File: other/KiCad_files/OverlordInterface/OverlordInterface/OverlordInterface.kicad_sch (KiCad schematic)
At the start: 8 parts, among them J1 Conn_01x12_Female, J2 DE9_Receptacle_MountingHoles_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, J3 DE9_Receptacle_MountingHoles_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, J4 DE9_Receptacle_MountingHoles_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, J5 DE9_Receptacle_MountingHoles_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

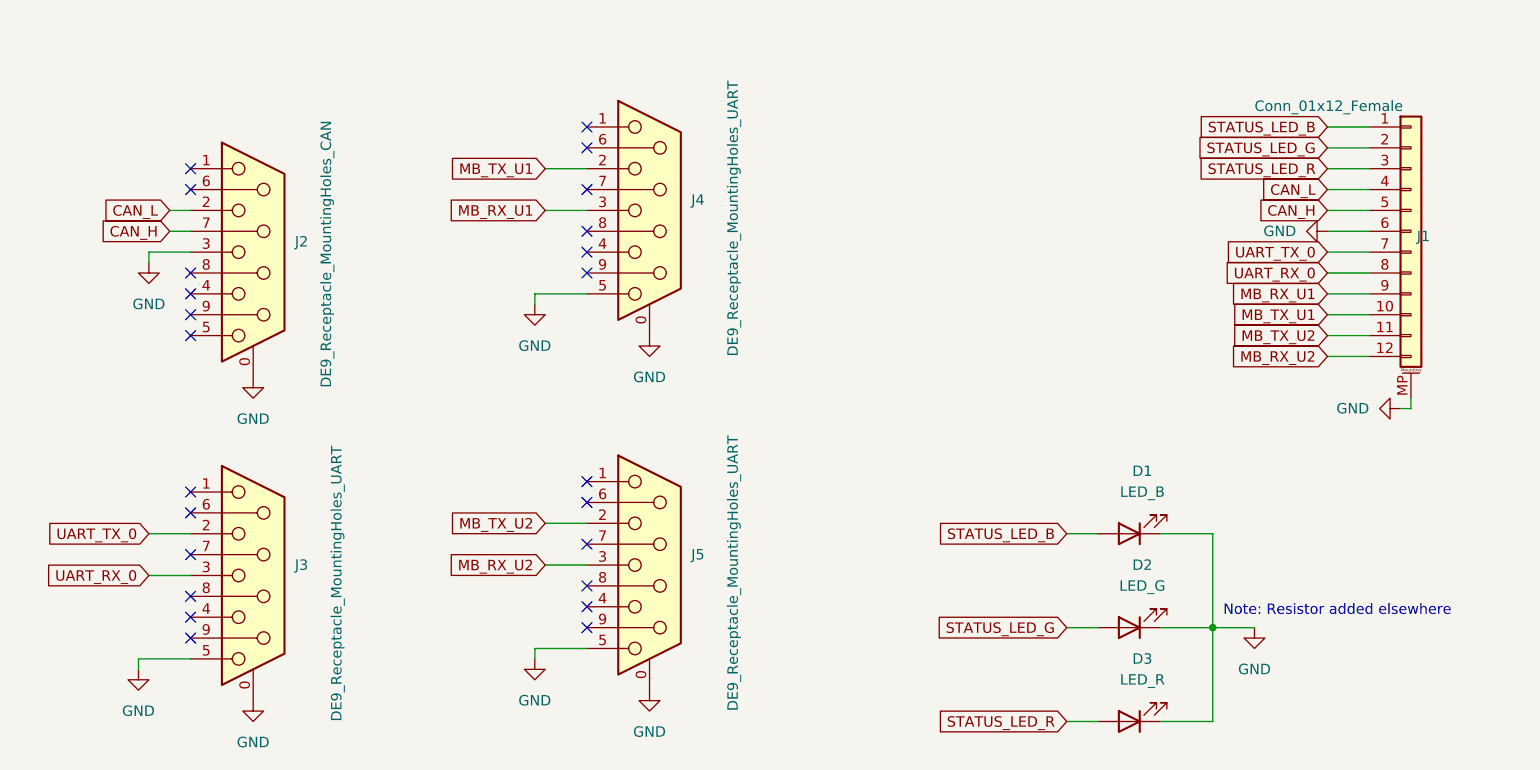
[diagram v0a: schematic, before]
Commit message: sent to production
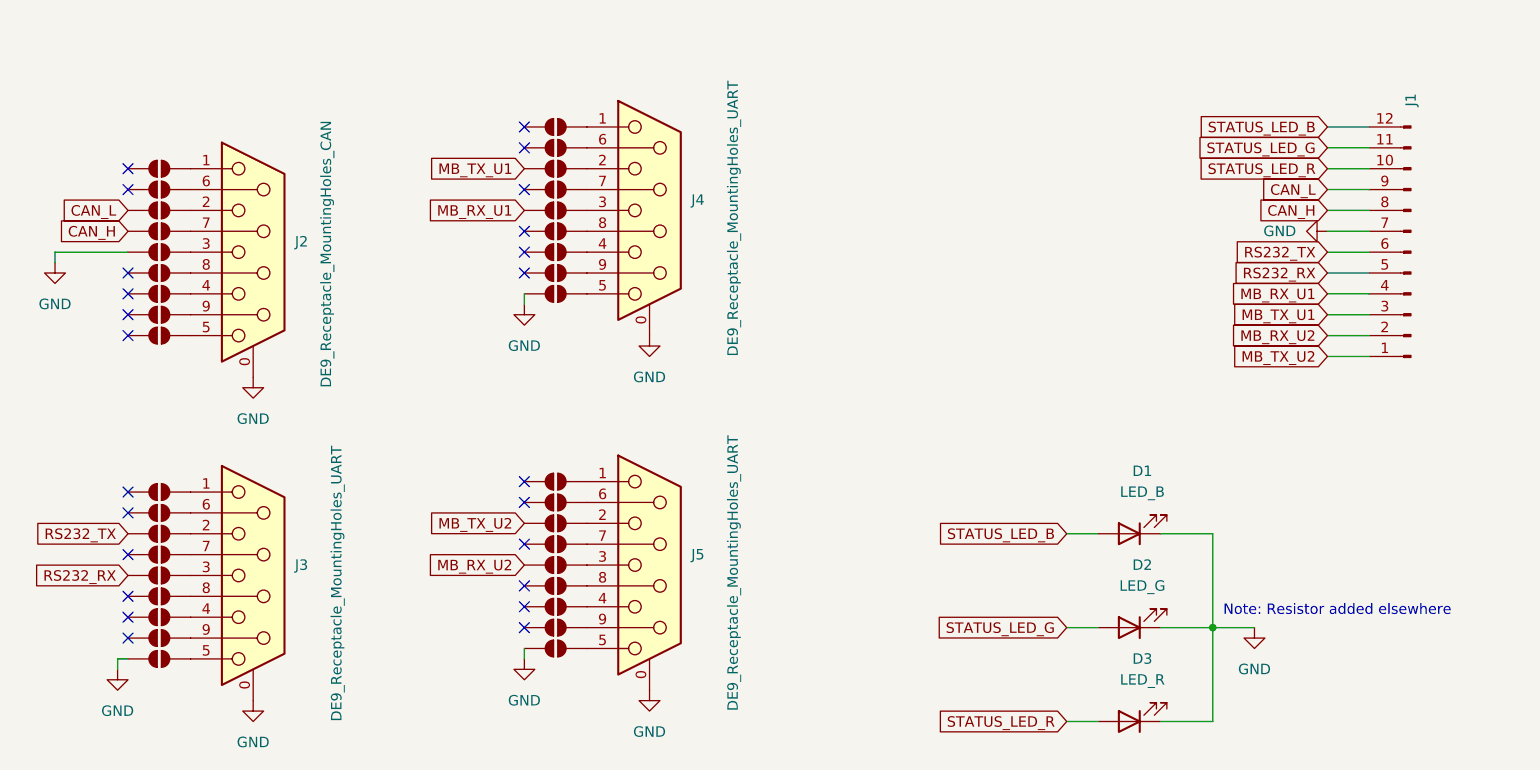
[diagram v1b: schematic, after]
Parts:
- removed J1: Conn_01x12_Female, Connector_Molex:Molex_CLIK-Mate_502386-1270_1x12-1MP_P1.25mm_Horizontal, symbol Connector_Generic_MountingPin:Conn_01x12_MountingPin
- added J1: Conn_01x12_Pin, Connector_Molex:Molex_Picoflex_90325-0012_2x06_P1.27mm_Vertical, symbol Connector:Conn_01x12_Pin
- added JP1, JP10, JP11, JP12, JP13, JP14, JP15, JP16, JP17, JP18, JP19, JP2, JP20, JP21, JP22, JP23, JP24, JP25, JP26, JP27, JP28, JP29, JP3, JP30, JP31, JP32, JP33, JP34, JP35, JP36, JP4, JP5, JP6, JP7, JP8, JP9: SolderJumper_2_Open, Jumper:SolderJumper-2_P1.3mm_Open_RoundedPad1.0x1.5mm, symbol Jumper:SolderJumper_2_Open
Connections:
- net CAN_H: now also J1.8 (Pin_8), JP12.1 (A); no longer J2.7
- net CAN_L: now also J1.9 (Pin_9), JP11.1 (A); no longer J2.2
- net GND: now also J1.7 (Pin_7), JP13.1 (A), JP26.1 (A), JP35.1 (A), JP36.1 (A); no longer J2.3, J3.5, J4.5, J5.5
- net MB_RX_U1: now also J1.4 (Pin_4), JP22.1 (A); no longer J4.3
- net MB_RX_U2: now also J1.2 (Pin_2), JP31.1 (A); no longer J5.3
- net MB_TX_U1: now also J1.3 (Pin_3), JP20.1 (A); no longer J4.2
- net MB_TX_U2: now also J1.1 (Pin_1), JP29.1 (A); no longer J5.2
- net STATUS_LED_B: now also J1.12 (Pin_12)
- net STATUS_LED_G: now also J1.11 (Pin_11)
- net STATUS_LED_R: now also J1.10 (Pin_10)
- net at J4.1: now also JP18.2 (B)
- net at J4.4: now also JP24.2 (B)
- net at J4.6: now also JP19.2 (B)
- net at J4.7: now also JP21.2 (B)
- net at J4.8: now also JP23.2 (B)
- net at J4.9: now also JP25.2 (B)
- net at J2.1: now also JP9.2 (B)
- net at J2.4: now also JP15.2 (B)
- net at J2.5: now also JP17.2 (B)
- net at J2.6: now also JP10.2 (B)
- net at J2.8: now also JP14.2 (B)
- net at J2.9: now also JP16.2 (B)
- net at J5.1: now also JP27.2 (B)
- net at J5.4: now also JP33.2 (B)
- net at J5.6: now also JP28.2 (B)
- net at J5.7: now also JP30.2 (B)
- net at J5.8: now also JP32.2 (B)
- net at J5.9: now also JP34.2 (B)
- net at J3.1: now also JP1.2 (B)
- net at J3.4: now also JP7.2 (B)
- net at J3.6: now also JP2.2 (B)
- net at J3.7: now also JP4.2 (B)
- net at J3.8: now also JP6.2 (B)
- net at J3.9: now also JP8.2 (B)
- net UART_RX_0: no longer names the net of J3.3
- net UART_RX_0: now also JP5.2 (B)
- net UART_TX_0: no longer names the net of J3.2
- net UART_TX_0: now also JP3.2 (B)
- new net: J4.3, JP22.2 (B)
- new net: J4.2, JP20.2 (B)
- new net: J5.2, JP29.2 (B)
- new net: J4.5, JP26.2 (B)
- new net: J2.2, JP11.2 (B)
- new net: J2.3, JP13.2 (B)
- new net: J2.7, JP12.2 (B)
- new net: J3.5, JP36.2 (B)
- new net: J5.3, JP31.2 (B)
- new net: J5.5, JP35.2 (B)
- new net RS232_RX: J1.5 (Pin_5), JP5.1 (A)
- new net RS232_TX: J1.6 (Pin_6), JP3.1 (A)
